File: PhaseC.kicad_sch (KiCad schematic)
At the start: 12 parts, among them Q10 Q_NMOS, Q9 Q_NMOS, U2 STDriveG600

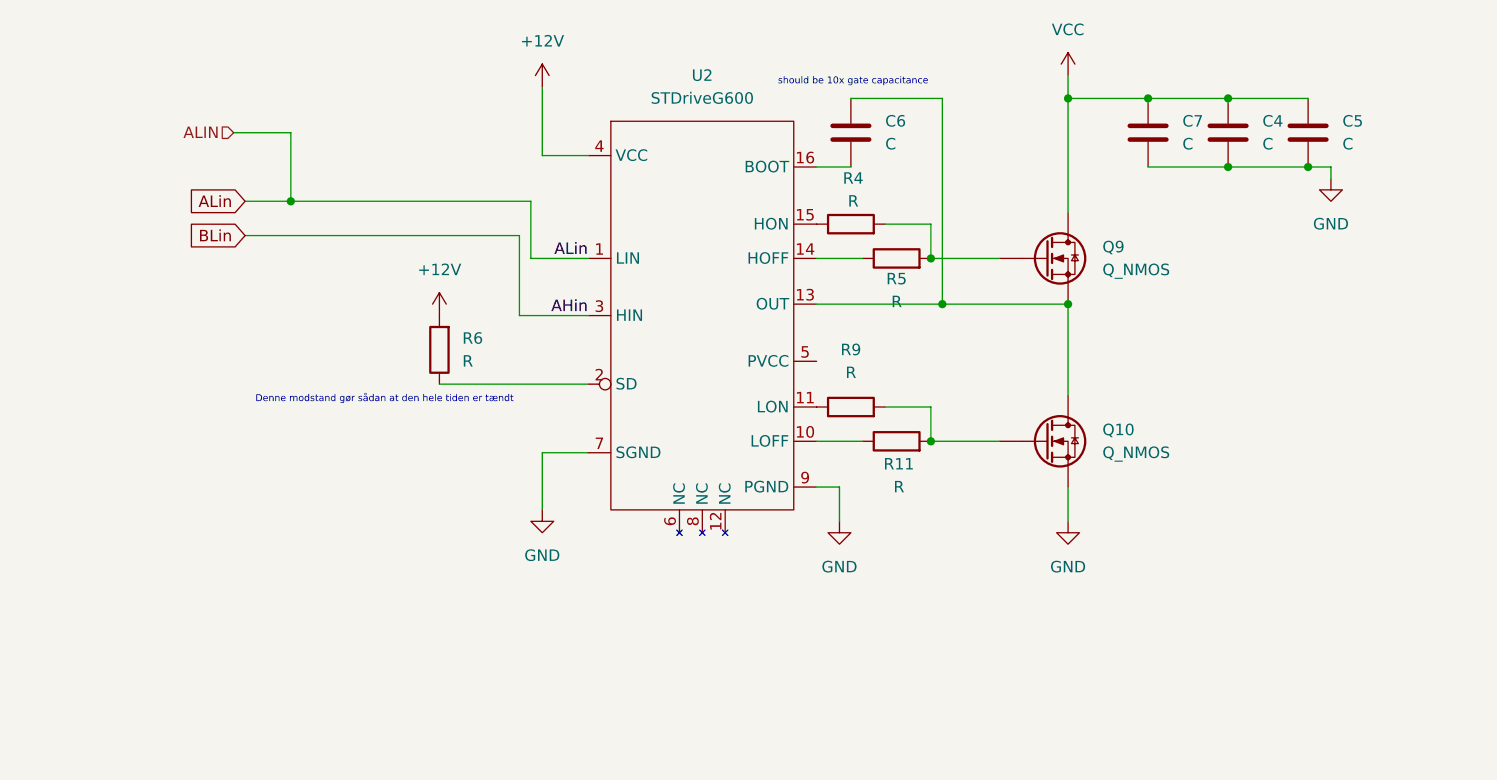
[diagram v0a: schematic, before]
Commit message: added hirearchical labels
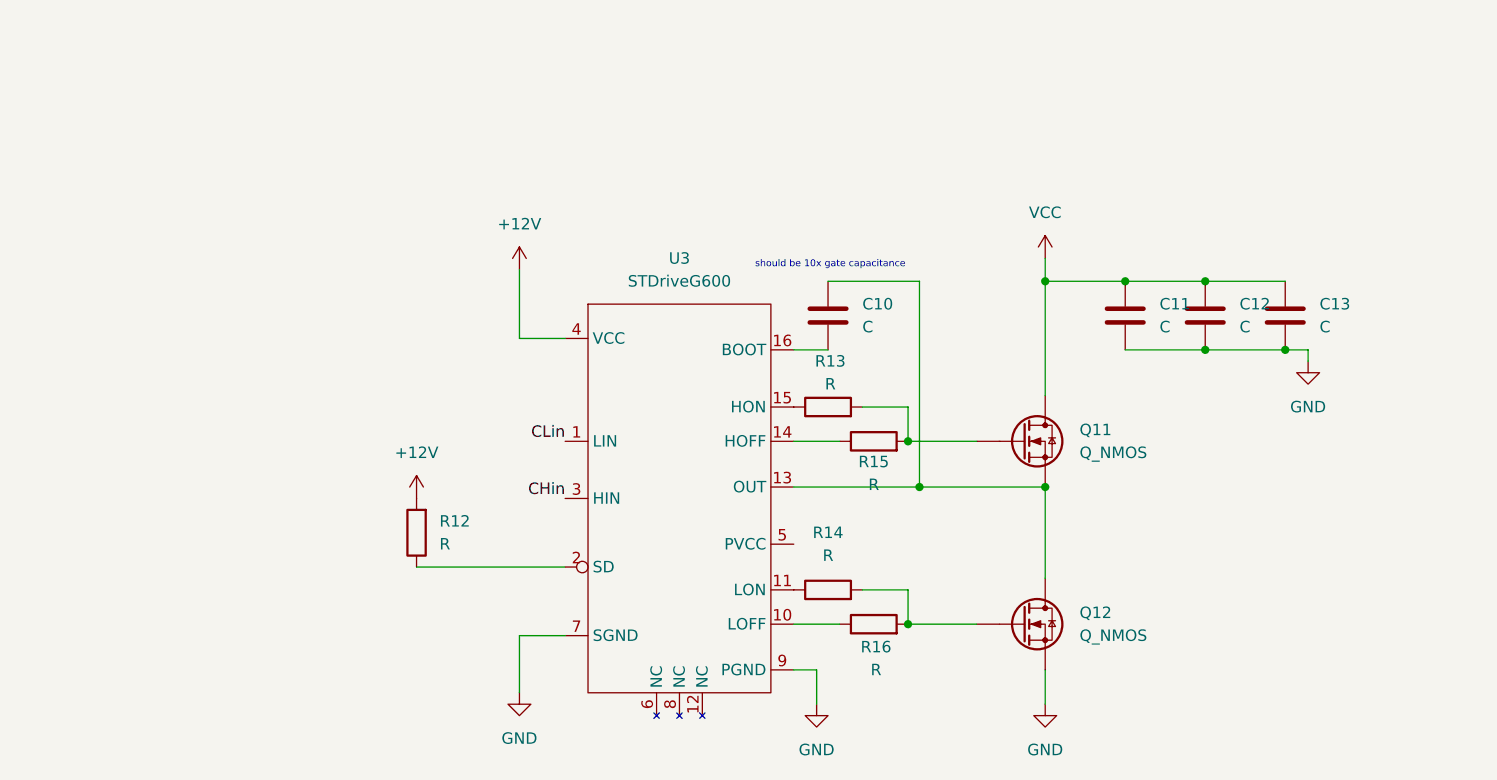
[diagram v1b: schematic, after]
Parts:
- removed C4, C5, C6, C7: C, symbol Device:C
- removed Q10, Q9: Q_NMOS, symbol Device:Q_NMOS
- removed R11, R4, R5, R6, R9: R, symbol Device:R
- removed U2: STDriveG600, Package_SO:SO-16_3.9x9.9mm_P1.27mm, symbol stm:STDRIVEG600
- added C10, C11, C12, C13: C, symbol Device:C
- added Q11, Q12: Q_NMOS, symbol Device:Q_NMOS
- added R12, R13, R14, R15, R16: R, symbol Device:R
- added U3: STDriveG600, Package_SO:SO-16_3.9x9.9mm_P1.27mm, symbol stm:STDRIVEG600
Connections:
- net +12V: now also R12.2, U3.4 (VCC)
- net GND: now also C11.2, C12.2, C13.2, Q12.S, U3.7 (SGND), U3.9 (PGND)
- net VCC: now also C11.1, C12.1, C13.1, Q11.D
- new net: C10.1, Q11.S, Q12.D, U3.13 (OUT)
- new net: Q12.G, R14.2, R16.2
- new net: R13.1, U3.15 (HON)
- new net: Q11.G, R13.2, R15.2
- new net: C10.2, U3.16 (BOOT)
- new net: R14.1, U3.11 (LON)
- new net: R16.1, U3.10 (LOFF)
- new net: R15.1, U3.14 (HOFF)
- new net: R12.1, U3.2 (SD)
- new net CHin: U3.3 (HIN)
- new net CLin: U3.1 (LIN)
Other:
- note removed: "Denne modstand gør sådan at den hele tiden er tændt"

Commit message: added more data for the 3 Phases. also added transformer
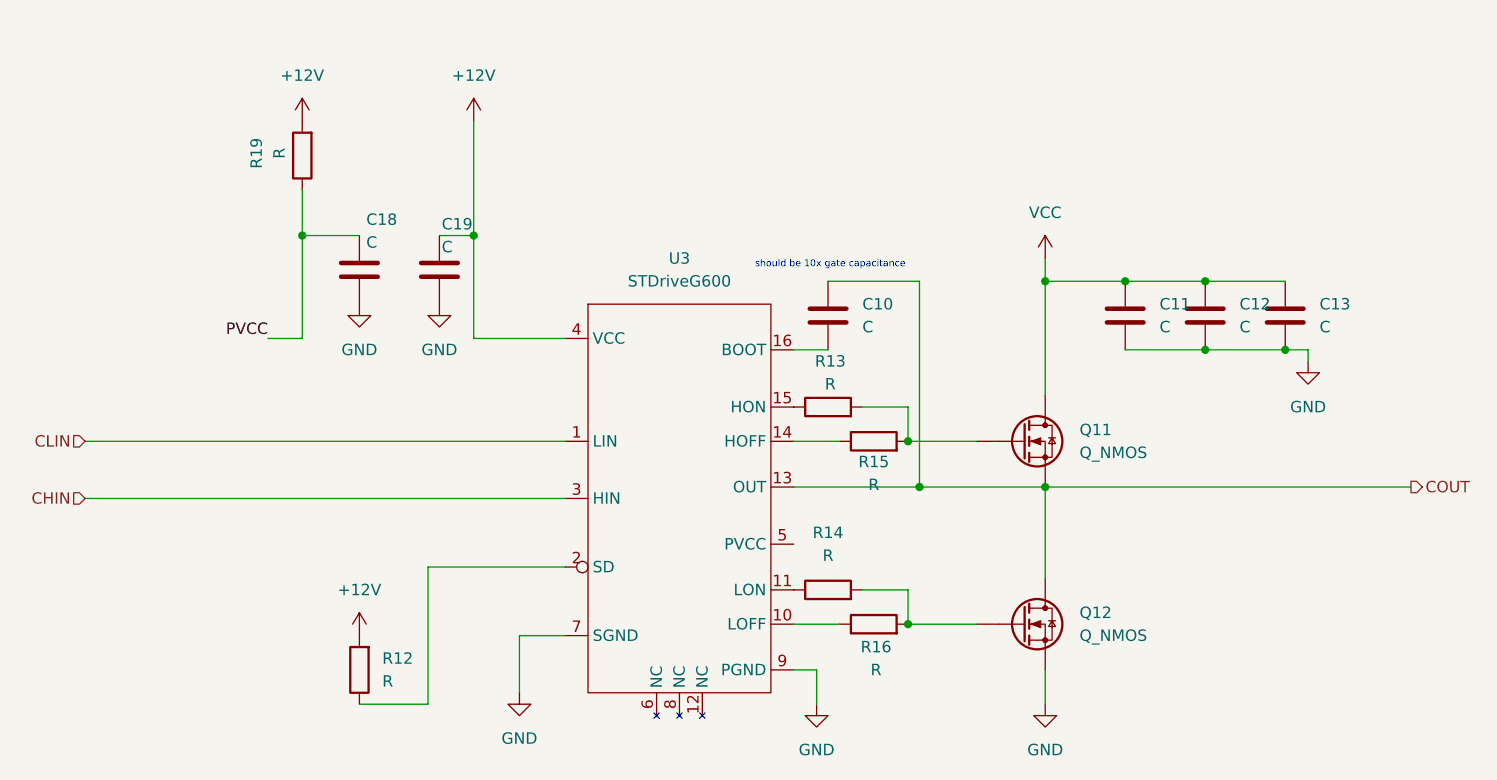
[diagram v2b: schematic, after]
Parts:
- added C18, C19: C, symbol Device:C
- added R19: R, symbol Device:R
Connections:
- net +12V: now also C19.1, R19.2
- net GND: now also C18.2, C19.2
- net COUT: now reaches C10.1, Q11.S, Q12.D, U3.13 (OUT)
- net CHin renamed CHIN
- net CLin renamed CLIN
- new net PVCC: C18.1, R19.1
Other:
- moved on the sheet: R12

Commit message: small changes
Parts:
- C10: value C -> 470n
- C11, C18, C19: value C -> 10u
- C12, C13: value C -> 100u
- R12: value R -> 10k
- R19: value R -> 3
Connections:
- net VCC renamed +48V
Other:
- note added: "flere typer kapacitorer husk strømvejen"

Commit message: added some kind of PCB design, a rough draft
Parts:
- removed Q11, Q12: Q_NMOS, symbol Device:Q_NMOS
- added Q15, Q16: C2M0025120D, Package_TO_SOT_THT:TO-247-3_Vertical, symbol Transistor_FET:C2M0025120D
- C14: renamed from C18; footprint (none) -> Capacitor_SMD:C_1812_4532Metric
- C15: renamed from C19; footprint (none) -> Capacitor_SMD:C_1812_4532Metric
- C16: renamed from C10; footprint (none) -> Capacitor_SMD:C_1206_3216Metric
- C17: renamed from C11; footprint (none) -> Capacitor_SMD:C_2220_5750Metric
- C18: renamed from C12; footprint (none) -> Capacitor_SMD:C_Elec_6.3x7.7
- C19: renamed from C13; footprint (none) -> Capacitor_SMD:C_Elec_6.3x7.7
- R14: renamed from R19; footprint (none) -> Resistor_SMD:R_1210_3225Metric
- R15: renamed from R13; footprint (none) -> Resistor_SMD:R_1206_3216Metric
- R16: renamed from R15; footprint (none) -> Resistor_SMD:R_1206_3216Metric
- R17: renamed from R14; footprint (none) -> Resistor_SMD:R_1206_3216Metric
- R18: renamed from R16; footprint (none) -> Resistor_SMD:R_1206_3216Metric
- R19: renamed from R12; footprint (none) -> Resistor_SMD:R_1812_4532Metric
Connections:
- net +48V: now also Q15.2 (D)
- net COUT: now also Q15.3 (S), Q16.2 (D)
- net GND: now also Q16.3 (S)
- net PVCC: now also U3.5 (PVCC)
- net at R17.2, R18.2: now also Q16.1 (G)
- net at R15.2, R16.2: now also Q15.1 (G)

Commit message: intial pcb layout
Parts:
- Q15, Q16: footprint Package_TO_SOT_THT:TO-247-3_Vertical -> Package_TO_SOT_SMD:TO-252-2
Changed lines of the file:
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@@
 			)
 		)
-		(property "Footprint" "Package_TO_SOT_THT:TO-247-3_Vertical"
+		(property "Footprint" "Package_TO_SOT_SMD:TO-252-2"
 			(at 172.72 92.075 0)
 			(effects
@@
 			)
 		)
-		(property "Footprint" "Package_TO_SOT_THT:TO-247-3_Vertical"
+		(property "Footprint" "Package_TO_SOT_SMD:TO-252-2"
 			(at 172.72 112.395 0)
 			(effects

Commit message: local restore changes
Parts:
- C14, C15: LCSC Part Number (none) -> C1021609
- C16: LCSC Part Number (none) -> C507059
- C17: LCSC Part Number (none) -> C2843466
- C18: value 100u -> 47u; footprint Capacitor_SMD:C_Elec_6.3x7.7 -> easyeda:CAP-SMD_BD6.3-L6.6-W6.6-LS7.3-FD; LCSC Part Number (none) -> C7461235
- C19: footprint Capacitor_SMD:C_Elec_6.3x7.7 -> easyeda:CAP-SMD_BD8.0-L8.3-W8.3-LS9.2-FD-H10.5; LCSC Part Number (none) -> C5456764
- Q15, Q16, R15, R16, R17, R18: now left out of the parts list
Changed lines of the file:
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@@
 		(unit 1)
 		(exclude_from_sim no)
-		(in_bom yes)
+		(in_bom no)
 		(on_board yes)
 		(dnp no)
@@
 		(unit 1)
 		(exclude_from_sim no)
-		(in_bom yes)
+		(in_bom no)
 		(on_board yes)
 		(dnp no)
@@
 		)
 		(property "Description" "Unpolarized capacitor"
+			(at 93.98 71.12 0)
+			(effects
+				(font
+					(size 1.27 1.27)
+				)
+				(hide yes)
+			)
+		)
+		(property "LCSC Part Number" "C1021609 "
 			(at 93.98 71.12 0)
 			(effects
@@
 			)
 		)
+		(property "LCSC Part Number" "C507059"
+			(at 146.05 76.2 0)
+			(effects
+				(font
+					(size 1.27 1.27)
+				)
+				(hide yes)
+			)
+		)
 		(pin "2"
 		)
@@
 		(unit 1)
 		(exclude_from_sim no)
-		(in_bom yes)
+		(in_bom no)
 		(on_board yes)
 		(dnp no)
@@
 			)
 		)
+		(property "LCSC Part Number" "C2843466"
+			(at 179.07 76.2 0)
+			(effects
+				(font
+					(size 1.27 1.27)
+				)
+				(hide yes)
+			)
+		)
 		(pin "1"
 		)
@@
 		(unit 1)
 		(exclude_from_sim no)
-		(in_bom yes)
+		(in_bom no)
 		(on_board yes)
 		(dnp no)
@@
 			)
 		)
-		(property "Value" "100u"
+		(property "Value" "47u"
 			(at 193.04 77.4699 0)
 			(effects
@@
 			)
 		)
-		(property "Footprint" "Capacitor_SMD:C_Elec_6.3x7.7"
+		(property "Footprint" "easyeda:CAP-SMD_BD6.3-L6.6-W6.6-LS7.3-FD"
 			(at 190.1952 80.01 0)
 			(effects
@@
 			)
 		)
+		(property "LCSC Part Number" "C7461235"
+			(at 189.23 76.2 0)
+			(effects
+				(font
+					(size 1.27 1.27)
+				)
+				(hide yes)
+			)
+		)
 		(pin "1"
 		)
@@
 		(unit 1)
 		(exclude_from_sim no)
-		(in_bom yes)
+		(in_bom no)
 		(on_board yes)
 		(dnp no)
@@
 		)
 		(property "Description" "Unpolarized capacitor"
+			(at 102.87 71.12 0)
+			(effects
+				(font
+					(size 1.27 1.27)
+				)
+				(hide yes)
+			)
+		)
+		(property "LCSC Part Number" "C1021609  "
 			(at 102.87 71.12 0)
 			(effects
@@
 		(unit 1)
 		(exclude_from_sim no)
-		(in_bom yes)
+		(in_bom no)
 		(on_board yes)
 		(dnp no)
@@
 			)
 		)
-		(property "Footprint" "Capacitor_SMD:C_Elec_6.3x7.7"
+		(property "Footprint" "easyeda:CAP-SMD_BD8.0-L8.3-W8.3-LS9.2-FD-H10.5"
 			(at 201.6252 80.01 0)
 			(effects
@@
 			(at 200.66 76.2 0)
 			(effects
+				(font
+					(size 1.27 1.27)
+				)
+				(hide yes)
+			)
+		)
+		(property "LCSC Part Number" "C5456764 "
+			(at 200.66 76.2 0)
+			(effects

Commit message: all små komponenter er nu 0805, og jeg har fixet strømmen under kondensatorerene, mangler kun at bytte rundt på 12Vin og GND
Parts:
- C14, C15: footprint Capacitor_SMD:C_1812_4532Metric -> Capacitor_SMD:C_0805_2012Metric_Pad1.18x1.45mm_HandSolder
- C16: footprint Capacitor_SMD:C_1206_3216Metric -> Capacitor_SMD:C_0805_2012Metric_Pad1.18x1.45mm_HandSolder
- R14: footprint Resistor_SMD:R_1210_3225Metric -> Resistor_SMD:R_0805_2012Metric_Pad1.20x1.40mm_HandSolder
- R15, R16, R17, R18: footprint Resistor_SMD:R_1206_3216Metric -> Resistor_SMD:R_0805_2012Metric_Pad1.20x1.40mm_HandSolder
- R19: footprint Resistor_SMD:R_1812_4532Metric -> Resistor_SMD:R_0805_2012Metric_Pad1.20x1.40mm_HandSolder
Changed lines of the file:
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@@
 			)
 		)
-		(property "Footprint" "Resistor_SMD:R_1210_3225Metric"
+		(property "Footprint" "Resistor_SMD:R_0805_2012Metric_Pad1.20x1.40mm_HandSolder"
 			(at 89.408 58.42 90)
 			(effects
@@
 			)
 		)
-		(property "Footprint" "Resistor_SMD:R_1206_3216Metric"
+		(property "Footprint" "Resistor_SMD:R_0805_2012Metric_Pad1.20x1.40mm_HandSolder"
 			(at 146.05 88.138 90)
 			(effects
@@
 			)
 		)
-		(property "Footprint" "Capacitor_SMD:C_1812_4532Metric"
+		(property "Footprint" "Capacitor_SMD:C_0805_2012Metric_Pad1.18x1.45mm_HandSolder"
 			(at 94.9452 74.93 0)
 			(effects
@@
 			)
 		)
-		(property "Footprint" "Capacitor_SMD:C_1206_3216Metric"
+		(property "Footprint" "Capacitor_SMD:C_0805_2012Metric_Pad1.18x1.45mm_HandSolder"
 			(at 147.0152 80.01 0)
 			(effects
@@
 			)
 		)
-		(property "Footprint" "Resistor_SMD:R_1206_3216Metric"
+		(property "Footprint" "Resistor_SMD:R_0805_2012Metric_Pad1.20x1.40mm_HandSolder"
 			(at 146.05 108.458 90)
 			(effects
@@
 			)
 		)
-		(property "Footprint" "Resistor_SMD:R_1812_4532Metric"
+		(property "Footprint" "Resistor_SMD:R_0805_2012Metric_Pad1.20x1.40mm_HandSolder"
 			(at 95.758 115.57 90)
 			(effects
@@
 			)
 		)
-		(property "Footprint" "Resistor_SMD:R_1206_3216Metric"
+		(property "Footprint" "Resistor_SMD:R_0805_2012Metric_Pad1.20x1.40mm_HandSolder"
 			(at 151.13 91.948 90)
 			(effects
@@
 			)
 		)
-		(property "Footprint" "Capacitor_SMD:C_1812_4532Metric"
+		(property "Footprint" "Capacitor_SMD:C_0805_2012Metric_Pad1.18x1.45mm_HandSolder"
 			(at 103.8352 74.93 0)
 			(effects
@@
 			)
 		)
-		(property "Footprint" "Resistor_SMD:R_1206_3216Metric"
+		(property "Footprint" "Resistor_SMD:R_0805_2012Metric_Pad1.20x1.40mm_HandSolder"
 			(at 151.13 112.268 90)
 			(effects

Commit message: Final Value Changes
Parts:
- Q15, Q16: value C2M0025120D -> FDD3672
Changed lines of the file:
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@@
 			)
 		)
-		(property "Value" "C2M0025120D"
+		(property "Value" "FDD3672"
 			(at 173.99 91.4399 0)
 			(effects
@@
 			)
 		)
-		(property "Datasheet" "https://www.wolfspeed.com/media/downloads/161/C2M0025120D.pdf"
+		(property "Datasheet" "https://www.onsemi.com/pdf/datasheet/fdd3672-d.pdf"
 			(at 172.72 93.98 0)
 			(effects
@@
 			)
 		)
-		(property "Description" "90A Id, 1200V Vds, 25mOhm, N-Channel SiC MOSFET, TO-247"
+		(property "Description" ""
 			(at 167.64 90.17 0)
 			(effects
@@
 			)
 		)
-		(property "Value" "C2M0025120D"
+		(property "Value" "FDD3672"
 			(at 173.99 111.7599 0)
 			(effects
@@
 			)
 		)
-		(property "Datasheet" "https://www.wolfspeed.com/media/downloads/161/C2M0025120D.pdf"
+		(property "Datasheet" "https://www.onsemi.com/pdf/datasheet/fdd3672-d.pdf"
 			(at 172.72 114.3 0)
 			(effects
@@
 			)
 		)
-		(property "Description" "90A Id, 1200V Vds, 25mOhm, N-Channel SiC MOSFET, TO-247"
+		(property "Description" ""
 			(at 167.64 110.49 0)
 			(effects
